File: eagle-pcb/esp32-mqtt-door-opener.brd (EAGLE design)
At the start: 53.3 x 53.3 mm, 14 parts, among them IC1 LM1117MP-3.3, K1 S202S02, U1 ESP-WROOM-32

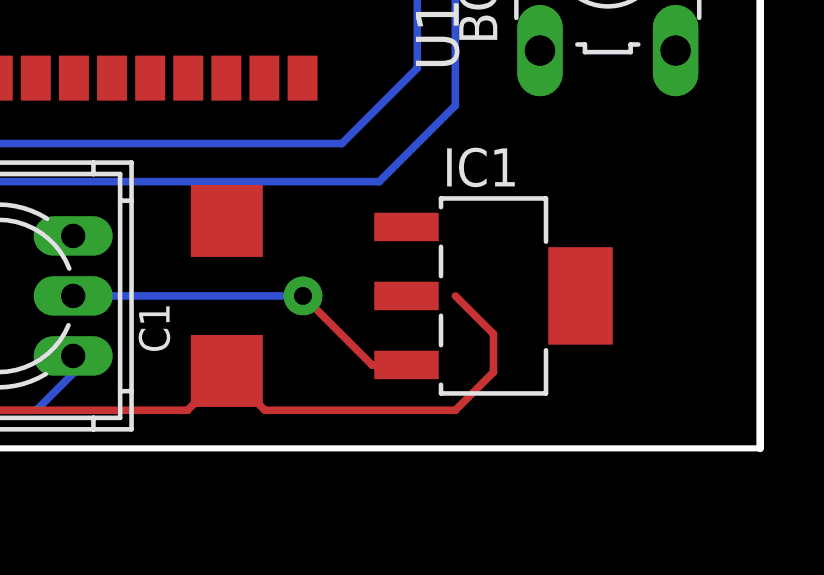
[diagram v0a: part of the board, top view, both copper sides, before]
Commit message: pcb: add missing trace
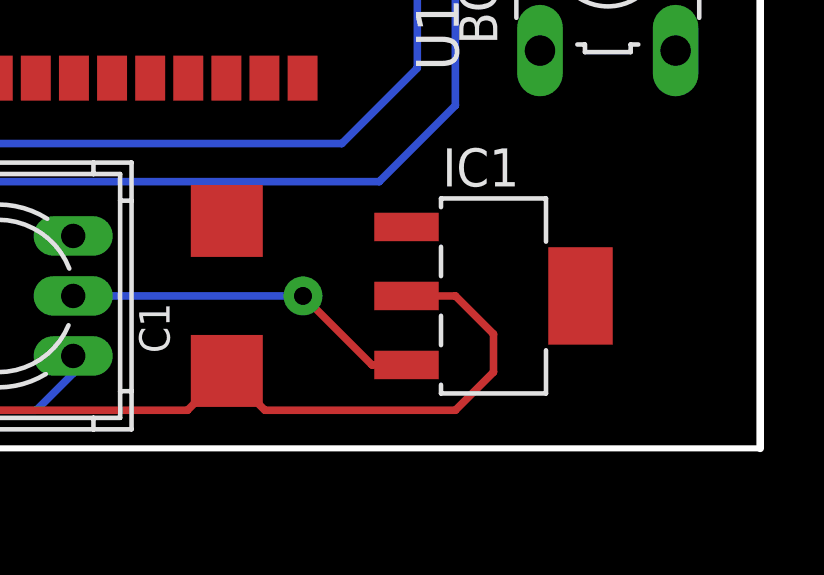
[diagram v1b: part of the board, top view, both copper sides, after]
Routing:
- net 3V3: track 57.7 -> 59.3 mm
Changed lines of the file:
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@@
 <wire x1="11.176" y1="16.51" x2="11.328" y2="16.358" width="0.1524" layer="1"/>
 <wire x1="11.328" y1="16.51" x2="11.176" y2="16.51" width="0.508" layer="1"/>
-<wire x1="43.18" y1="5.08" x2="44.45" y2="3.81" width="0.254" layer="1"/>
+<wire x1="44.45" y1="3.81" x2="43.18" y2="5.08" width="0.254" layer="1"/>
 <wire x1="44.45" y1="3.81" x2="44.45" y2="2.54" width="0.254" layer="1"/>
 <wire x1="44.45" y1="2.54" x2="43.18" y2="1.27" width="0.254" layer="1"/>
@@
 <wire x1="36.83" y1="1.27" x2="35.54" y2="2.56" width="0.254" layer="1"/>
 <wire x1="43.18" y1="1.27" x2="36.83" y2="1.27" width="0.254" layer="1"/>
-<wire x1="43.18" y1="5.08" x2="47.35" y2="5.08" width="0" layer="19" extent="1-1"/>
-<wire x1="41.55" y1="5.08" x2="43.18" y2="5.08" width="0" layer="19" extent="1-1"/>
+<wire x1="43.18" y1="5.08" x2="41.55" y2="5.08" width="0.254" layer="1"/>
+<wire x1="41.55" y1="5.08" x2="47.35" y2="5.08" width="0" layer="19" extent="1-1"/>
 </signal>
 <signal name="~2">

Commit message: pcb: stretch power source lane
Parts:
- moved IC1 3.81 mm to (48.3, 5.08)
- moved C1 2.54 mm to (38.1, 5.08)
- moved S1 2.54 mm to (30.5, 5.08)
- moved B1 1.37 mm to (16.5, 4.57)
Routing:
- net 3V3: track 59.3 -> 62.4 mm
- net ~1: track 5.68 -> 7.16 mm
- net ~2: track 5.68 -> 7.15 mm
- net ON/OFF: track 12.1 -> 13.5 mm
- net VCC: track 12.3 -> 13.5 mm

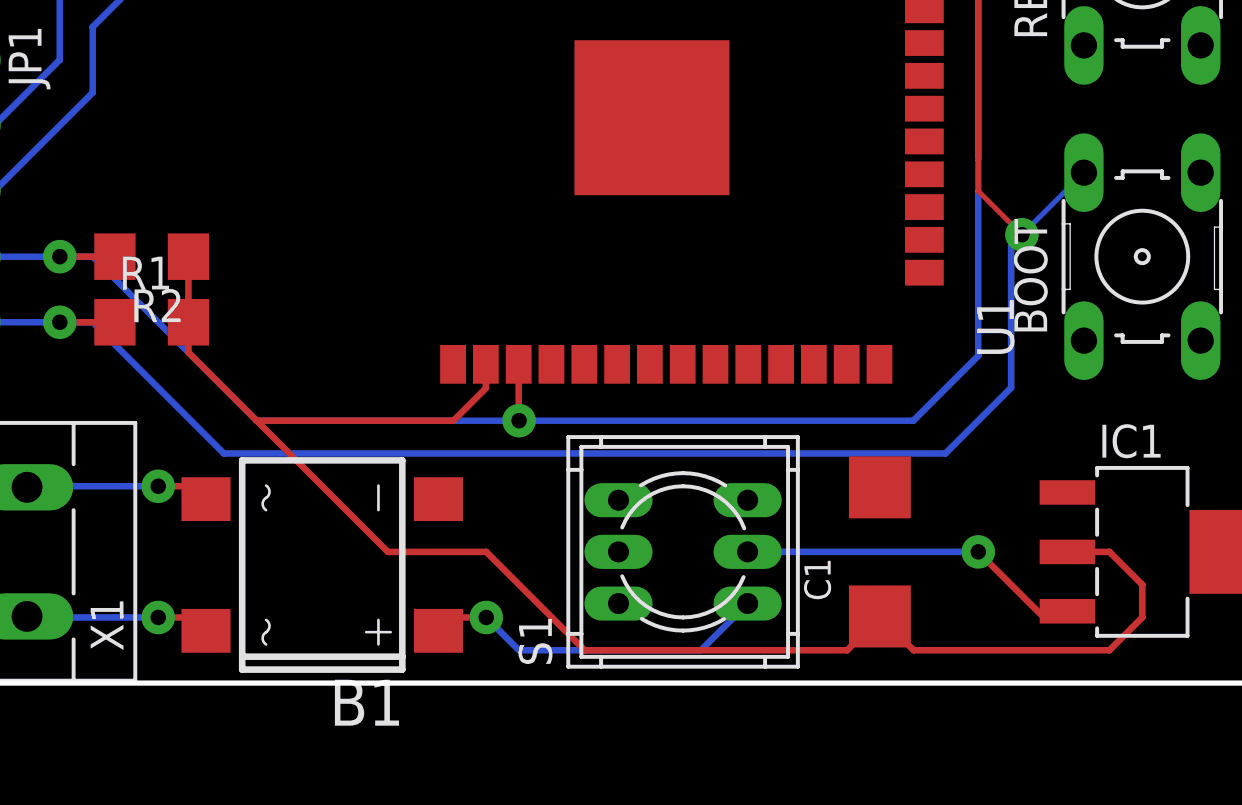
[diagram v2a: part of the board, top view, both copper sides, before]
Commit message: pcb: change wire widths and move rectifier a bit
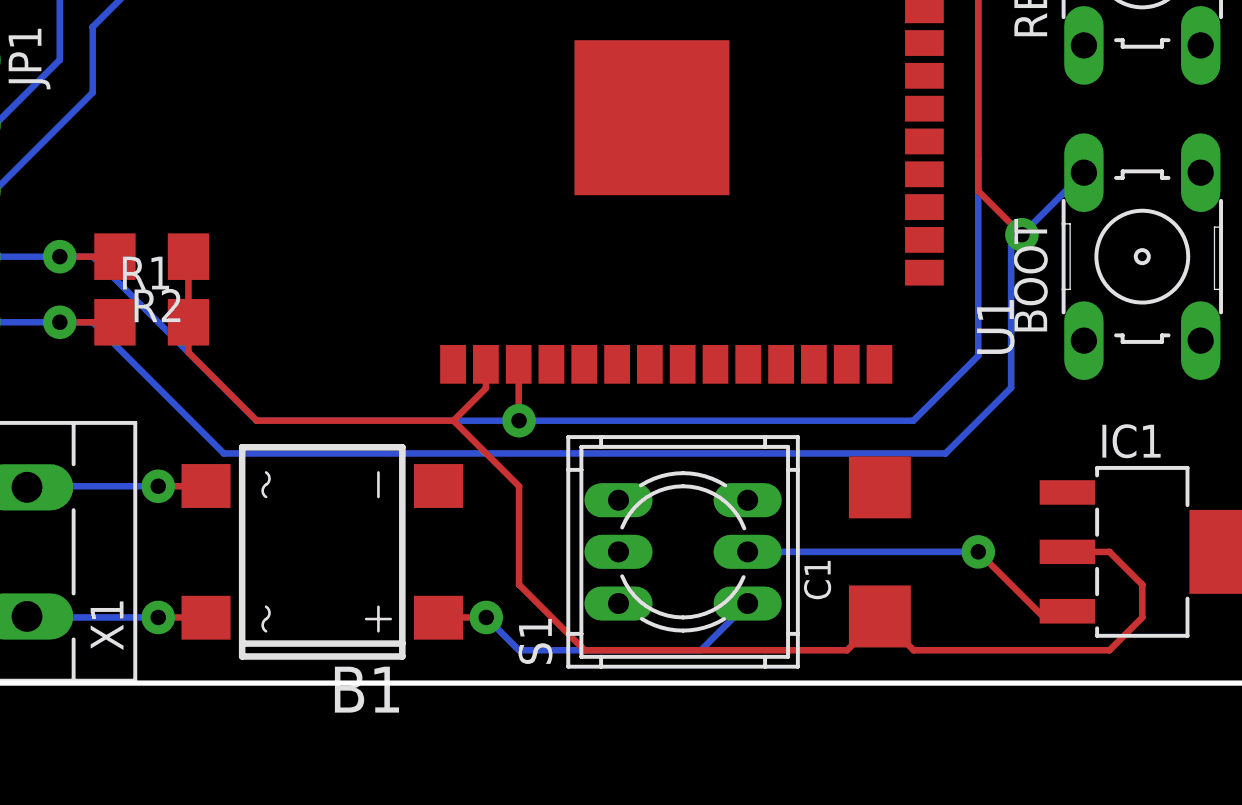
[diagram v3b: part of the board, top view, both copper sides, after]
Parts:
- moved B1 0.51 mm to (16.5, 5.08)
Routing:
- net 3V3: track 62.4 -> 57.0 mm
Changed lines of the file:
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@@
 </autorouter>
 <elements>
-<element name="B1" library="rectifier" library_urn="urn:adsk.eagle:library:336" package="DBS" package3d_urn="urn:adsk.eagle:package:23898/1" value="DBS107G" x="16.51" y="4.572" smashed="yes" rot="R90">
-<attribute name="NAME" x="19.685" y="0.127" size="1.778" layer="25" ratio="10" rot="R180"/>
-<attribute name="POPULARITY" value="0" x="49.53" y="40.132" size="1.778" layer="27" rot="R90" display="off"/>
-<attribute name="VALUE" x="17.145" y="1.397" size="1.778" layer="27" ratio="10" rot="R90"/>
+<element name="B1" library="rectifier" library_urn="urn:adsk.eagle:library:336" package="DBS" package3d_urn="urn:adsk.eagle:package:23898/1" value="DBS107G" x="16.51" y="5.08" smashed="yes" rot="R90">
+<attribute name="NAME" x="19.685" y="0.635" size="1.778" layer="25" ratio="10" rot="R180"/>
+<attribute name="POPULARITY" value="0" x="49.53" y="40.64" size="1.778" layer="27" rot="R90" display="off"/>
+<attribute name="VALUE" x="17.145" y="1.905" size="1.778" layer="27" ratio="10" rot="R90"/>
 </element>
 <element name="BOOT" library="switch-omron" library_urn="urn:adsk.eagle:library:377" package="B3F-10XX" package3d_urn="urn:adsk.eagle:package:27496/1" value="" x="48.26" y="16.51" smashed="yes" rot="R90">
@@
 <wire x1="41.91" y1="29.21" x2="40.28" y2="30.84" width="0.254" layer="1"/>
 <wire x1="40.28" y1="30.84" x2="38.085" y2="30.84" width="0.254" layer="1"/>
-<wire x1="43.18" y1="16.9418" x2="43.5991" y2="17.3609" width="0.2" layer="16"/>
+<wire x1="43.18" y1="16.9418" x2="43.5991" y2="17.3609" width="0.254" layer="16"/>
 <via x="43.5991" y="17.3609" extent="1-16" drill="0.6" diameter="1.3"/>
-<wire x1="45.9994" y1="19.7612" x2="43.5991" y2="17.3609" width="0.2" layer="16"/>
-<wire x1="43.5991" y1="17.3609" x2="41.91" y2="19.05" width="0.2" layer="1"/>
-<wire x1="41.91" y1="19.05" x2="41.91" y2="20.32" width="0.2" layer="1"/>
+<wire x1="45.9994" y1="19.7612" x2="43.5991" y2="17.3609" width="0.254" layer="16"/>
+<wire x1="43.5991" y1="17.3609" x2="41.91" y2="19.05" width="0.254" layer="1"/>
+<wire x1="41.91" y1="19.05" x2="41.91" y2="20.32" width="0.254" layer="1"/>
 </signal>
 <signal name="OUT">
@@
 <wire x1="11.328" y1="12.802" x2="11.328" y2="13.97" width="0.254" layer="1"/>
 <wire x1="11.328" y1="12.802" x2="13.97" y2="10.16" width="0.254" layer="1"/>
-<wire x1="13.97" y1="10.16" x2="19.05" y2="5.08" width="0.254" layer="1"/>
-<wire x1="19.05" y1="5.08" x2="22.86" y2="5.08" width="0.254" layer="1"/>
 <contactref element="IC1" pad="4"/>
 <contactref element="IC1" pad="2"/>
@@
 <wire x1="39.41" y1="1.27" x2="38.12" y2="2.56" width="0.254" layer="1"/>
 <wire x1="38.12" y1="2.56" x2="38.1" y2="2.58" width="0.254" layer="1"/>
-<wire x1="22.86" y1="5.08" x2="26.67" y2="1.27" width="0.254" layer="1"/>
-<wire x1="26.67" y1="1.27" x2="36.83" y2="1.27" width="0.254" layer="1"/>
+<wire x1="36.83" y1="1.27" x2="26.67" y2="1.27" width="0.254" layer="1"/>
 <wire x1="36.83" y1="1.27" x2="38.12" y2="2.56" width="0.254" layer="1"/>
+<wire x1="26.67" y1="1.27" x2="24.13" y2="3.81" width="0.254" layer="1"/>
+<wire x1="24.13" y1="3.81" x2="24.13" y2="7.62" width="0.254" layer="1"/>
+<wire x1="24.13" y1="7.62" x2="21.59" y2="10.16" width="0.254" layer="1"/>
 <wire x1="45.36" y1="5.08" x2="51.16" y2="5.08" width="0" layer="19" extent="1-1"/>
 </signal>
@@
 <wire x1="10.16" y1="7.62" x2="5.12" y2="7.62" width="0.254" layer="16"/>
 <wire x1="5.12" y1="7.62" x2="5.08" y2="7.58" width="0.254" layer="16"/>
-<wire x1="10.16" y1="7.62" x2="11.512" y2="7.62" width="0.254" layer="1"/>
-<wire x1="11.512" y1="7.62" x2="12.01" y2="7.122" width="0.254" layer="1"/>
+<wire x1="10.16" y1="7.62" x2="12" y2="7.62" width="0.254" layer="1"/>
+<wire x1="12" y1="7.62" x2="12.01" y2="7.63" width="0.254" layer="1"/>
 </signal>
 <signal name="~1">
@@
 <contactref element="B1" pad="AC1"/>
 <via x="10.16" y="2.54" extent="1-16" drill="0.6" diameter="1.3"/>
-<wire x1="10.16" y1="2.54" x2="11.492" y2="2.54" width="0.254" layer="1"/>
-<wire x1="11.492" y1="2.54" x2="12.01" y2="2.022" width="0.254" layer="1"/>
+<wire x1="10.16" y1="2.54" x2="12" y2="2.54" width="0.254" layer="1"/>
+<wire x1="12" y1="2.54" x2="12.01" y2="2.53" width="0.254" layer="1"/>
 <wire x1="10.16" y1="2.54" x2="5.12" y2="2.54" width="0.254" layer="16"/>
 <wire x1="5.12" y1="2.54" x2="5.08" y2="2.58" width="0.254" layer="16"/>
@@
 <contactref element="B1" pad="+"/>
 <contactref element="S1" pad="4"/>
-<wire x1="21.01" y1="2.022" x2="21.528" y2="2.54" width="0.254" layer="1"/>
-<wire x1="21.528" y1="2.54" x2="22.86" y2="2.54" width="0.254" layer="1"/>
+<wire x1="21.01" y1="2.53" x2="21.02" y2="2.54" width="0.254" layer="1"/>
+<wire x1="21.02" y1="2.54" x2="22.86" y2="2.54" width="0.254" layer="1"/>
 <via x="22.86" y="2.54" extent="1-16" drill="0.6" diameter="1.3"/>
 <wire x1="22.86" y1="2.54" x2="24.13" y2="1.27" width="0.254" layer="16"/>

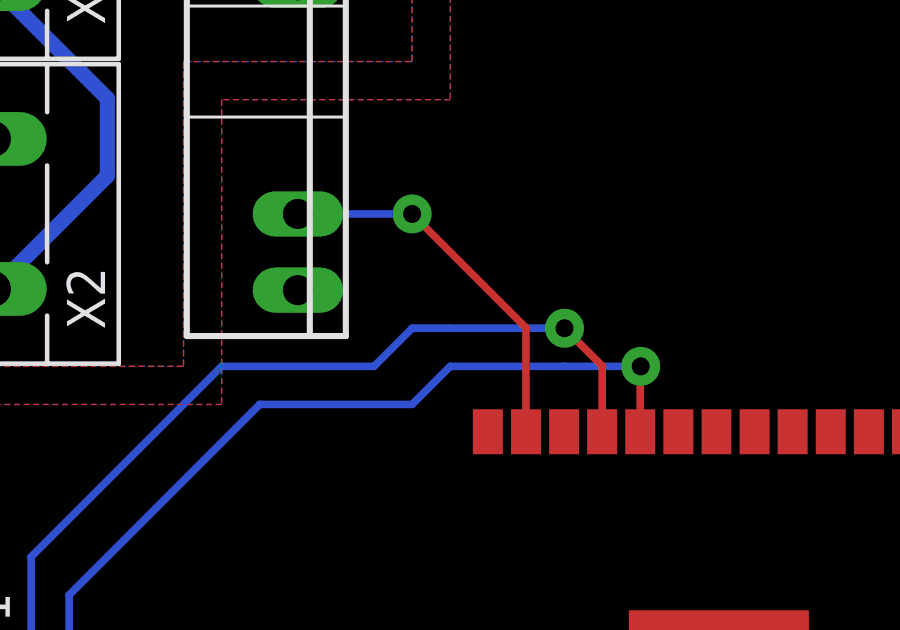
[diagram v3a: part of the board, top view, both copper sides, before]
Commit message: pcb: minor improvements to trace routing
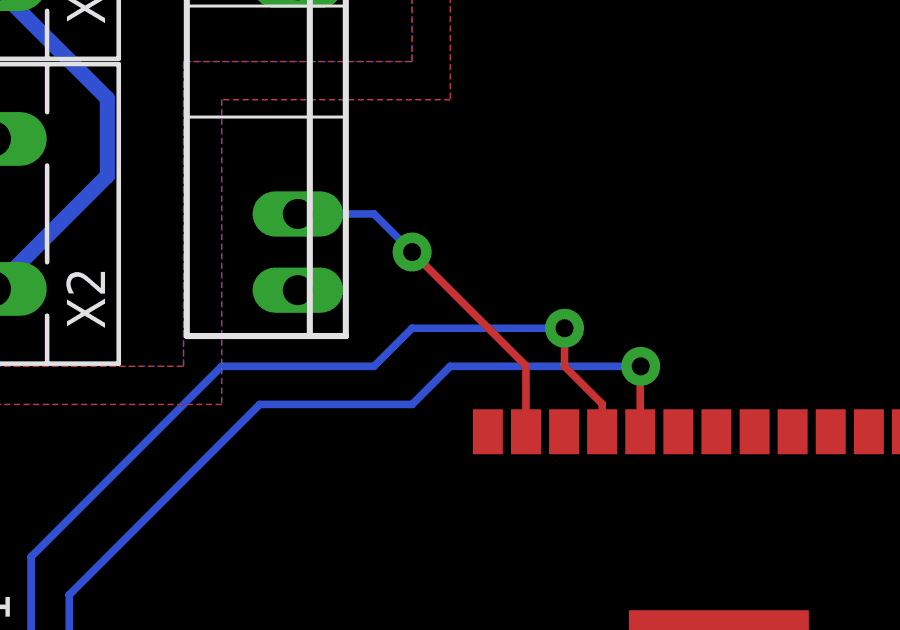
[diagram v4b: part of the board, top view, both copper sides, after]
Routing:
- net GPIO23: track 12.6 -> 11.9 mm
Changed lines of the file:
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@@
 <contactref element="JP1" pad="2"/>
 <contactref element="U1" pad="35"/>
-<wire x1="25.385" y1="30.84" x2="25.385" y2="33.035" width="0.254" layer="1"/>
-<wire x1="25.385" y1="33.035" x2="24.13" y2="34.29" width="0.254" layer="1"/>
 <via x="24.13" y="34.29" extent="1-16" drill="0.6" diameter="1.3"/>
-<wire x1="24.13" y1="34.29" x2="20.32" y2="34.29" width="0.254" layer="16"/>
-<wire x1="20.32" y1="34.29" x2="19.05" y2="34.29" width="0.254" layer="16"/>
+<wire x1="24.13" y1="34.29" x2="19.05" y2="34.29" width="0.254" layer="16"/>
 <wire x1="19.05" y1="34.29" x2="17.78" y2="33.02" width="0.254" layer="16"/>
 <wire x1="17.78" y1="33.02" x2="12.7" y2="33.02" width="0.254" layer="16"/>
@@
 <wire x1="6.35" y1="24.13" x2="3.81" y2="21.59" width="0.254" layer="16"/>
 <wire x1="3.81" y1="21.59" x2="2.54" y2="21.59" width="0.254" layer="16"/>
+<wire x1="25.385" y1="30.84" x2="25.385" y2="31.765" width="0.254" layer="1"/>
+<wire x1="25.385" y1="31.765" x2="24.13" y2="33.02" width="0.254" layer="1"/>
+<wire x1="24.13" y1="33.02" x2="24.13" y2="34.29" width="0.254" layer="1"/>
 </signal>
 <signal name="RX">
@@
 <contactref element="U1" pad="37"/>
 <contactref element="K1" pad="3"/>
-<wire x1="22.845" y1="30.84" x2="22.845" y2="34.305" width="0.254" layer="1"/>
-<wire x1="22.845" y1="34.305" x2="19.05" y2="38.1" width="0.254" layer="1"/>
-<via x="19.05" y="38.1" extent="1-16" drill="0.6" diameter="1.3"/>
-<wire x1="19.05" y1="38.1" x2="15.24" y2="38.1" width="0.254" layer="16"/>
+<wire x1="22.845" y1="30.84" x2="22.845" y2="33.035" width="0.254" layer="1"/>
+<wire x1="22.845" y1="33.035" x2="19.05" y2="36.83" width="0.254" layer="1"/>
+<via x="19.05" y="36.83" extent="1-16" drill="0.6" diameter="1.3"/>
+<wire x1="19.05" y1="36.83" x2="17.78" y2="38.1" width="0.254" layer="16"/>
+<wire x1="17.78" y1="38.1" x2="15.24" y2="38.1" width="0.254" layer="16"/>
 </signal>
 <signal name="ON/OFF">

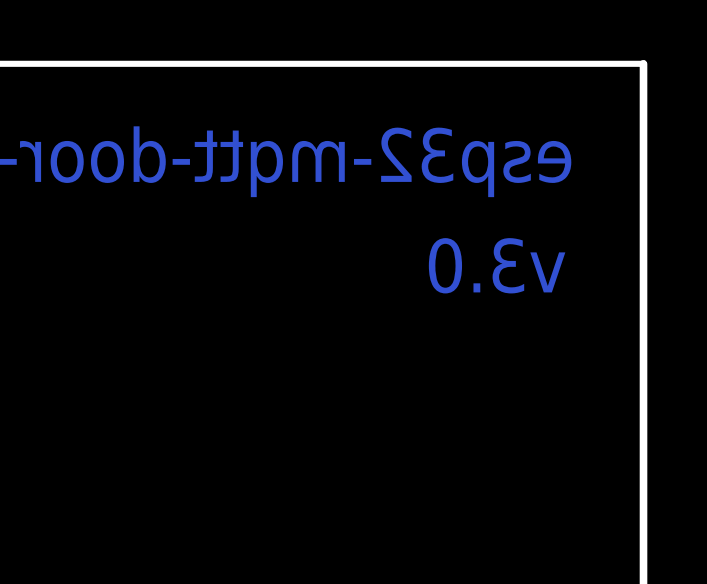
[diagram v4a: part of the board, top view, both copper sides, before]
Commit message: pcb: revision 3.1 with rubout incoming
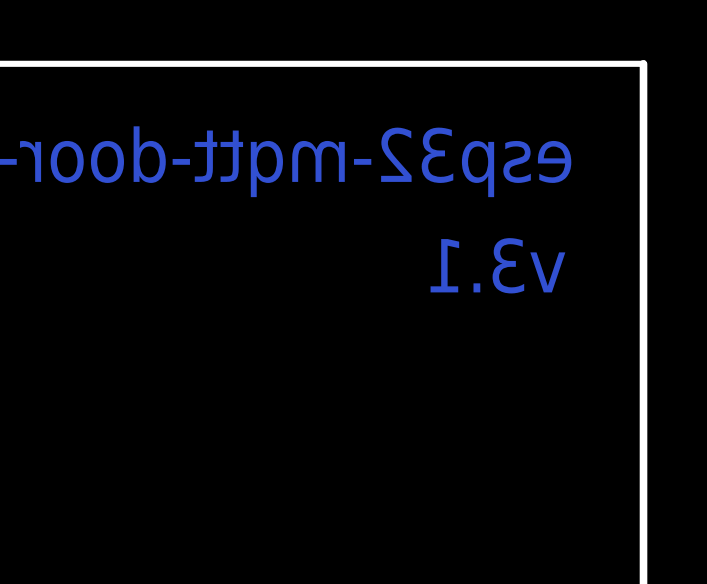
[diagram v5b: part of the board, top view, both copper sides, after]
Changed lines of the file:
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@@
 </plain>
 <attributes>
-<attribute name="CREVISION" value="3.0"/>
+<attribute name="CREVISION" value="3.1"/>
 </attributes>
 <variantdefs>
